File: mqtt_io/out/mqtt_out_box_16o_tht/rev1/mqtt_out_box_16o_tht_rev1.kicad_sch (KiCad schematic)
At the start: 139 parts, among them J1 Conn_01x04_Pin, J18 Conn_01x04_Pin, J19 Conn_01x02_Pin, K1 FINDER-40.31, K10 FINDER-40.31, K11 FINDER-40.31, K12 FINDER-40.31, K13 FINDER-40.31, K14 FINDER-40.31, K15 FINDER-40.31, K16 FINDER-40.31, K2 FINDER-40.31, K3 FINDER-40.31, K4 FINDER-40.31, K5 FINDER-40.31, K6 FINDER-40.31, K7 FINDER-40.31, K8 FINDER-40.31, K9 FINDER-40.31, Q1 IRFZ24N, U1 MCP23017_SP

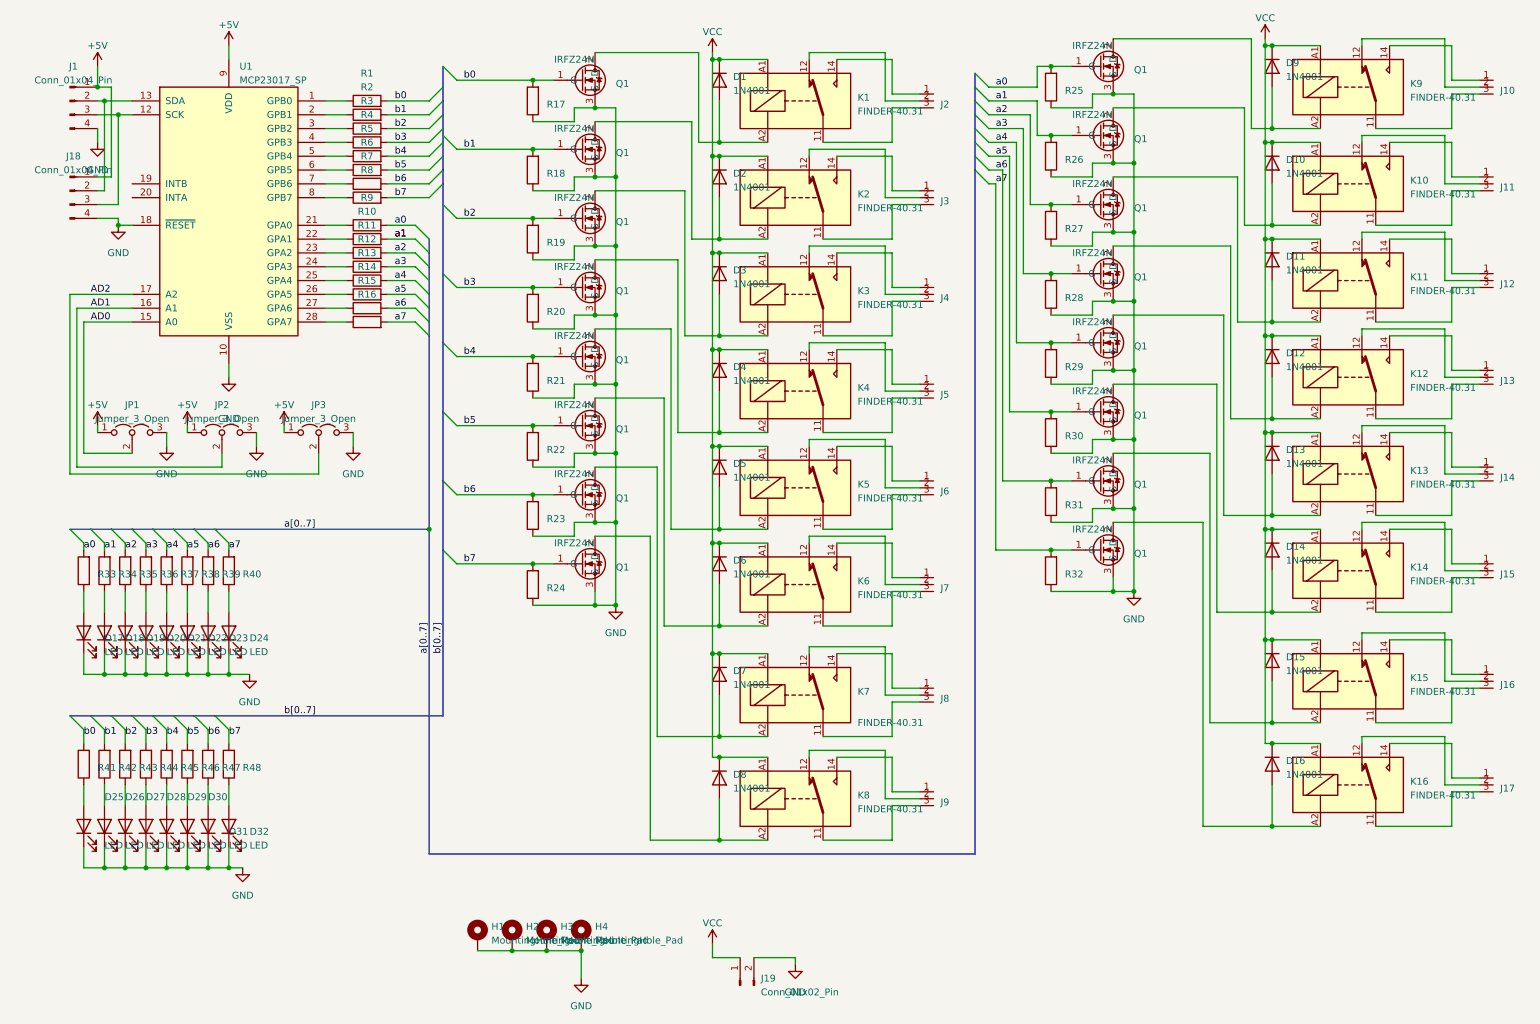
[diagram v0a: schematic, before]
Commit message: Pullup für ic2 eingefügt (4k7)
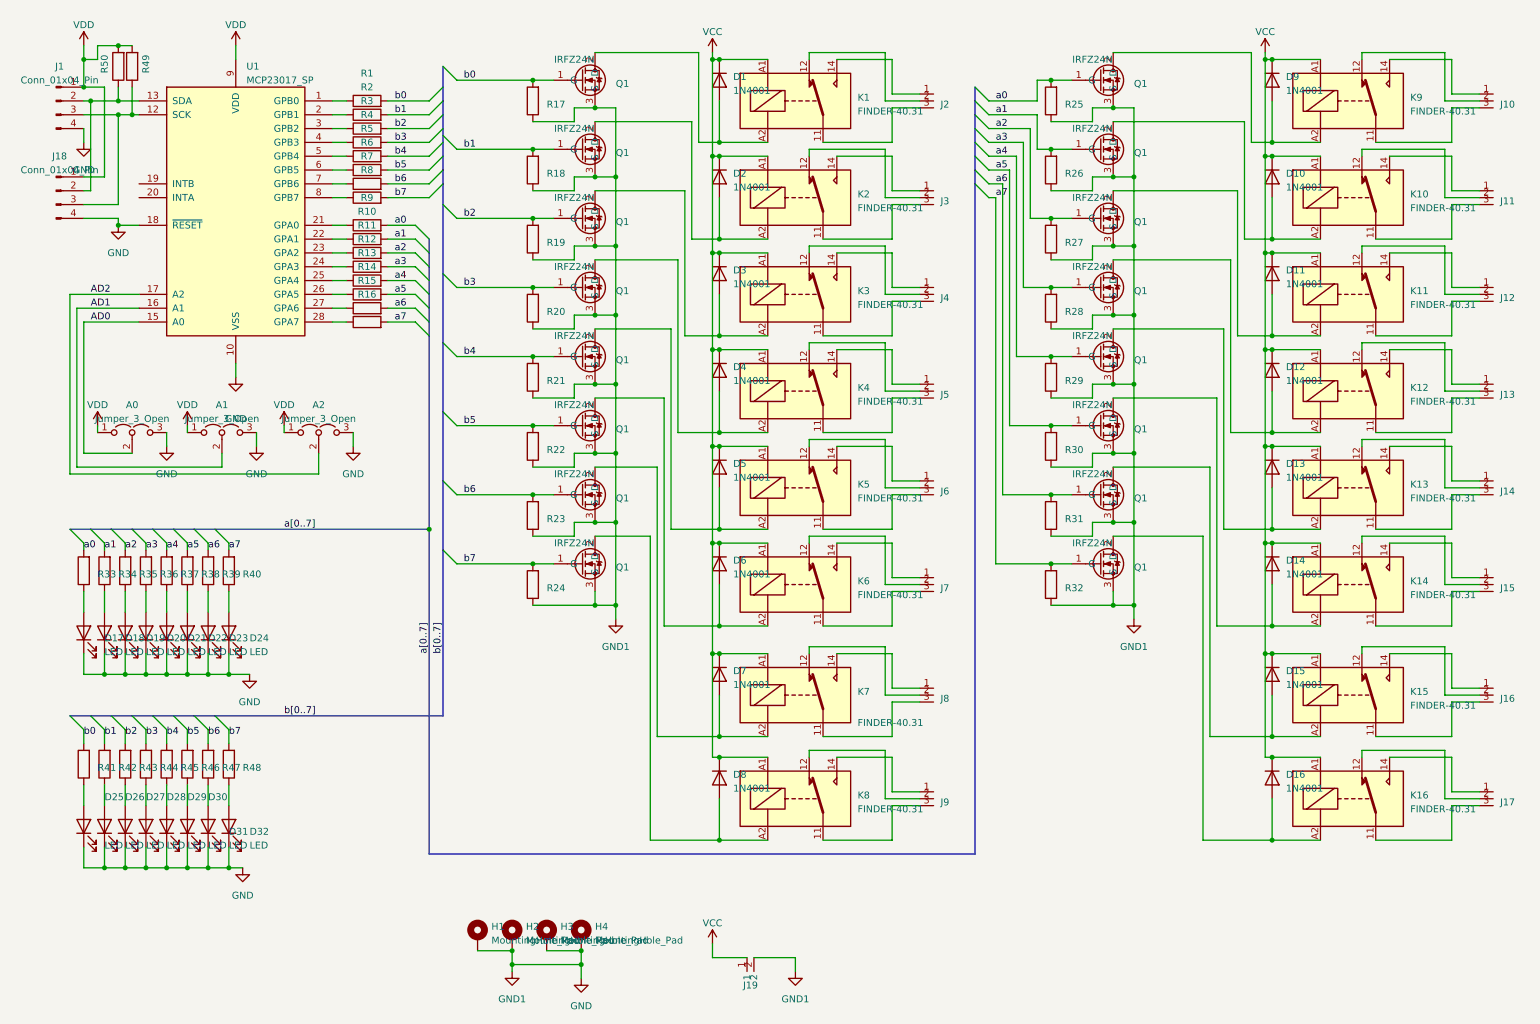
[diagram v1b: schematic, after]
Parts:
- removed J19: Conn_01x02_Pin, Connector_PinHeader_2.54mm:PinHeader_1x02_P2.54mm_Vertical, symbol Connector:Conn_01x02_Pin
- added J19: ~, parts_tma_1:AST_041-2, symbol parts_tma_1:AST_041-2
- added R49, R50: 4k7, Resistor_THT:R_Axial_DIN0204_L3.6mm_D1.6mm_P7.62mm_Horizontal, symbol Device:R
- renumbered JP1 to A0, JP2 to A1, JP3 to A2
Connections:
- net GND: now also J19.2
- net VCC: now also J19.1
- net at J1.3 (Pin_3), J18.3 (Pin_3), U1.12 (SCK): now also R49.1
- net at J1.2 (Pin_2), J18.2 (Pin_2), U1.13 (SDA): now also R50.1
- net +5V renamed VDD
- net VDD: now also R49.2, R50.2
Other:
- moved on the sheet: D10, D11, D12, D13, D14, D15, D16, D9, J1, J10, J11, J12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

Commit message: neue Dateien eingefügt.
out Platine rev 2, testprogramm für pi pico
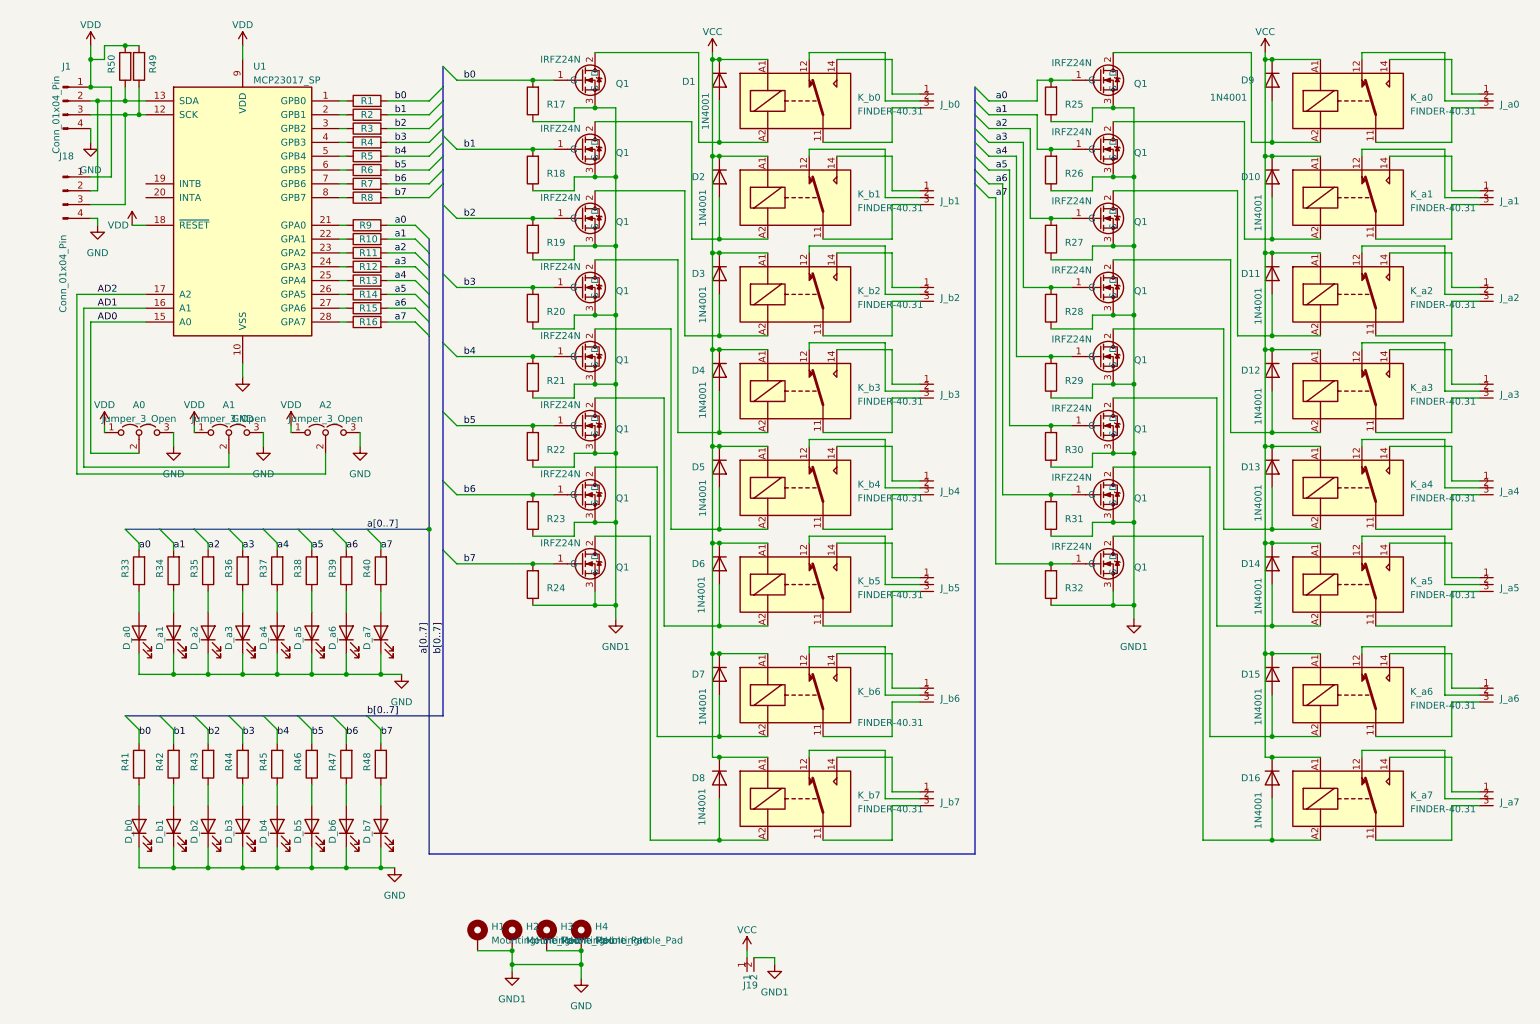
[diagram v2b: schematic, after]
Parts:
- renumbered D17 to D_a0, D18 to D_a1, D19 to D_a2, D20 to D_a3, D21 to D_a4, D22 to D_a5, D23 to D_a6, D24 to D_a7, D25 to D_b0, D26 to D_b1, D27 to D_b2, D28 to D_b3, D29 to D_b4, D30 to D_b5, D31 to D_b6, D32 to D_b7, J10 to J_a0, J11 to J_a1, J12 to J_a2, J13 to J_a3, J14 to J_a4, J15 to J_a5, J16 to J_a6, J17 to J_a7, J2 to J_b0, J3 to J_b1, J4 to J_b2, J5 to J_b3, J6 to J_b4, J7 to J_b5, J8 to J_b6, J9 to J_b7, K9 to K_a0, K10 to K_a1, K11 to K_a2, K12 to K_a3, K13 to K_a4, K14 to K_a5, K15 to K_a6, K16 to K_a7, K1 to K_b0, K2 to K_b1, K3 to K_b2, K4 to K_b3, K5 to K_b4, K6 to K_b5, K7 to K_b6, K8 to K_b7
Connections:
- net GND: no longer U1.18 (~{RESET})
- net VDD: now also U1.18 (~{RESET})
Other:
- moved on the sheet: A0, A1, A2, D_a0, D_a1, D_a2, D_a3, D_a4, D_a5, D_a6, D_a7, D_b0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
